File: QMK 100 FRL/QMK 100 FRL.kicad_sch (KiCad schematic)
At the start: 26 parts, among them J2 SM04B-SRSS-TB

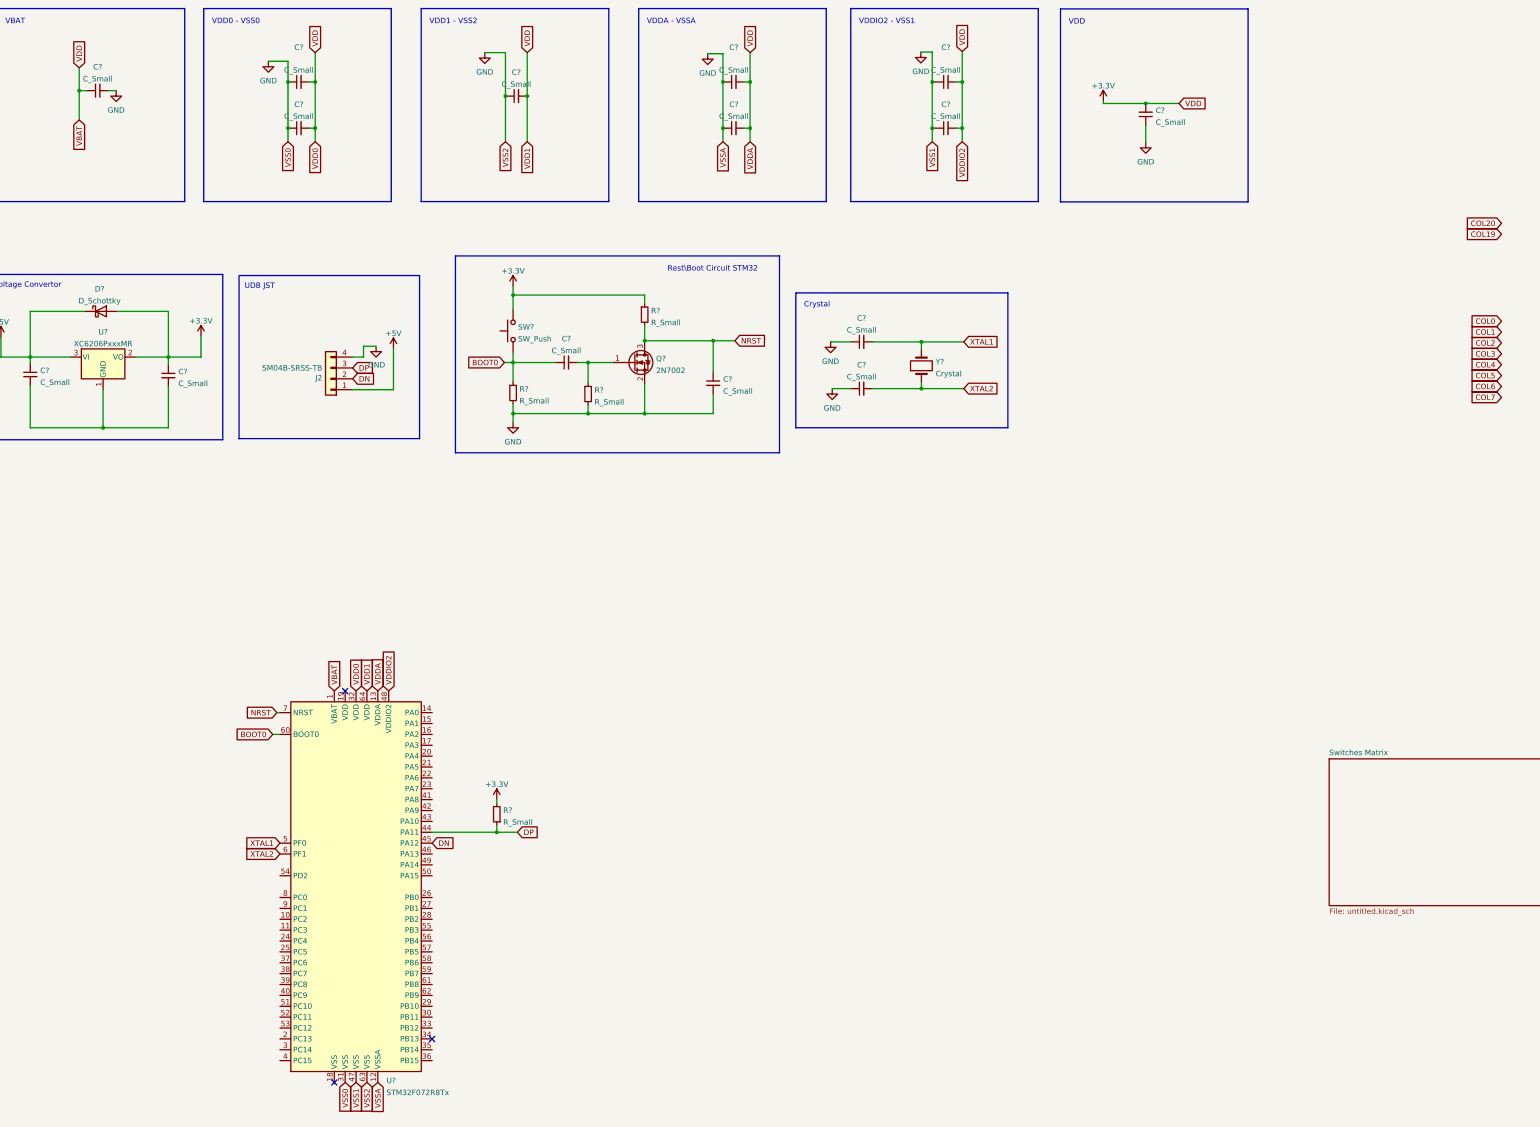
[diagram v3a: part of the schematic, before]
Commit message: Updated the pcb schema
Updated the pcb with a new schema as i am still studying\developing a new pcb for qmak board.
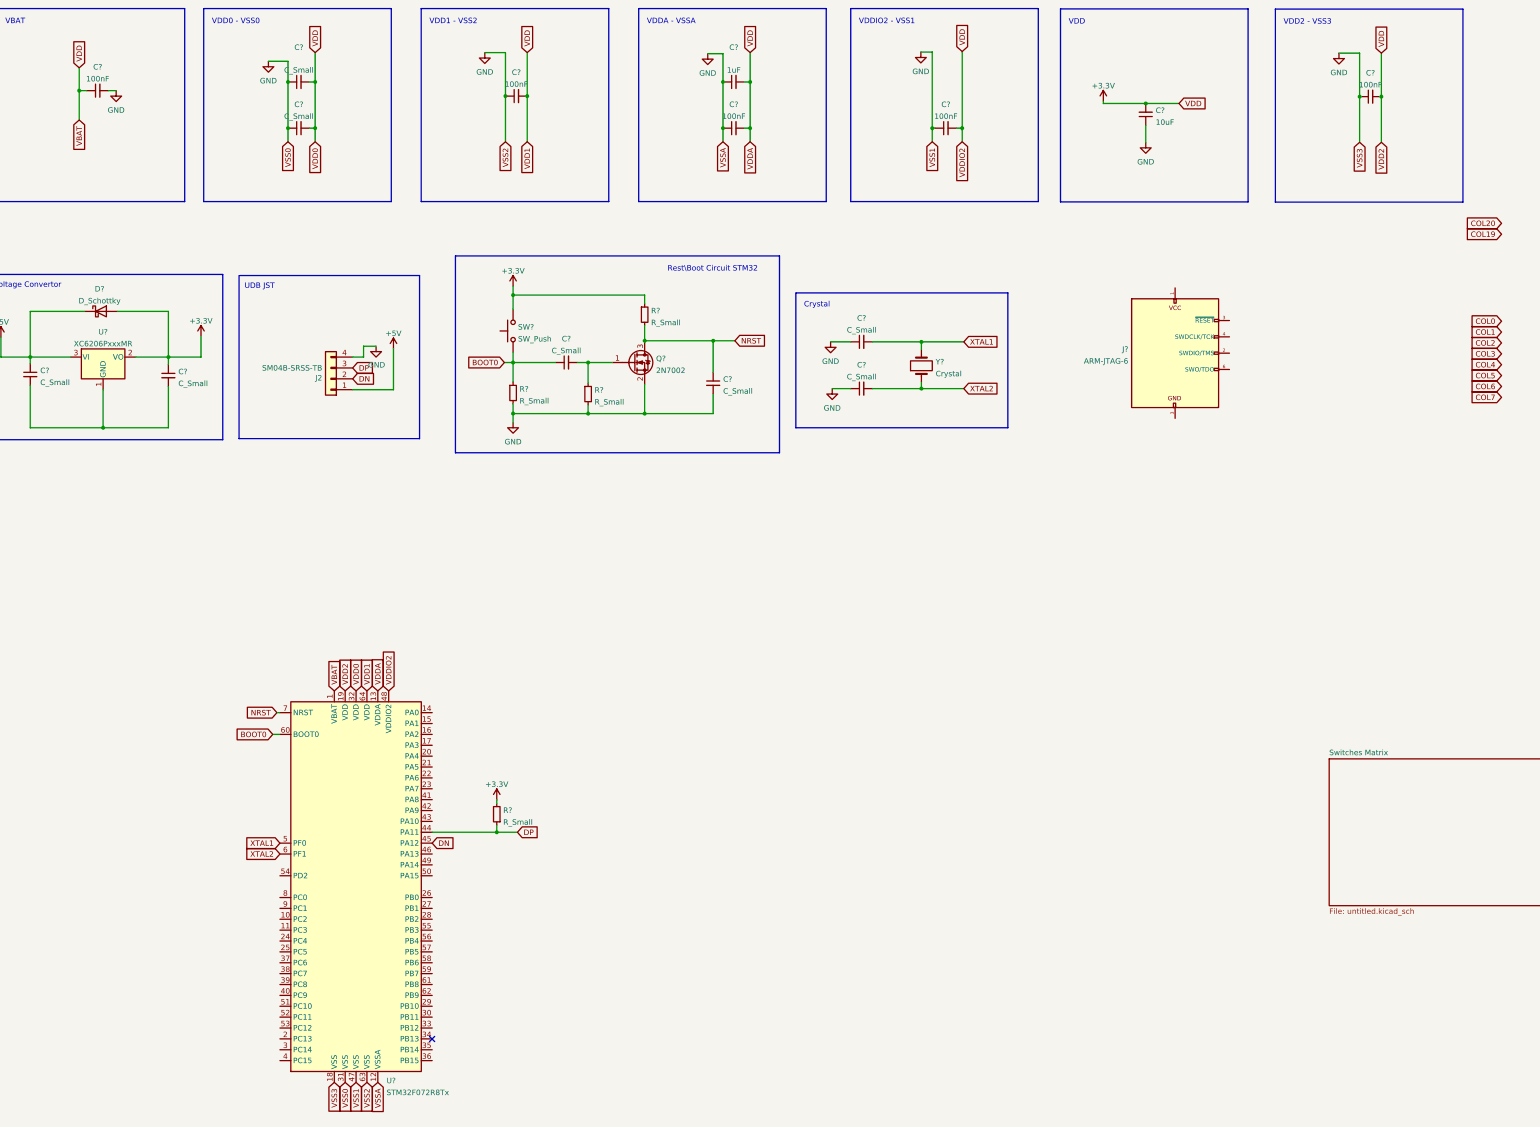
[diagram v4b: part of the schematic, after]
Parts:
- removed C?: C_Small, symbol Device:C_Small
- added C?: 100nF, symbol Device:C_Small
- added J?: ARM-JTAG-6, symbol acheronSymbols:ARM-JTAG-6
- C?: value C_Small -> 1uF
- C? (x4): value C_Small -> 100nF
- C?: value C_Small -> 10uF
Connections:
- net +3V3: now also U?.19 (VDD), C?.2
- net GND: now also U?.18 (VSS), C?.1
- new net: J?.3 (~{RESET}), J?.5 (GND)
- no-connect marks 3 -> 1
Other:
- note added: "VDD2 - VSS3"
